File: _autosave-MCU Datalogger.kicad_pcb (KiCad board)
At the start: 2 copper layers, 50.8 x 31.9 mm, 30 parts, among them J1 Conn_01x04_Pin, J2 Conn_01x04_Pin, J3 Conn_01x09_Pin, J4 Conn_02x03_Odd_Even, U1 24LC1025, U2 24LC1025, U3 ATMEGA328P-AU, U4 DS1337S_, Y1 32.768kHz, Y2 16KHz

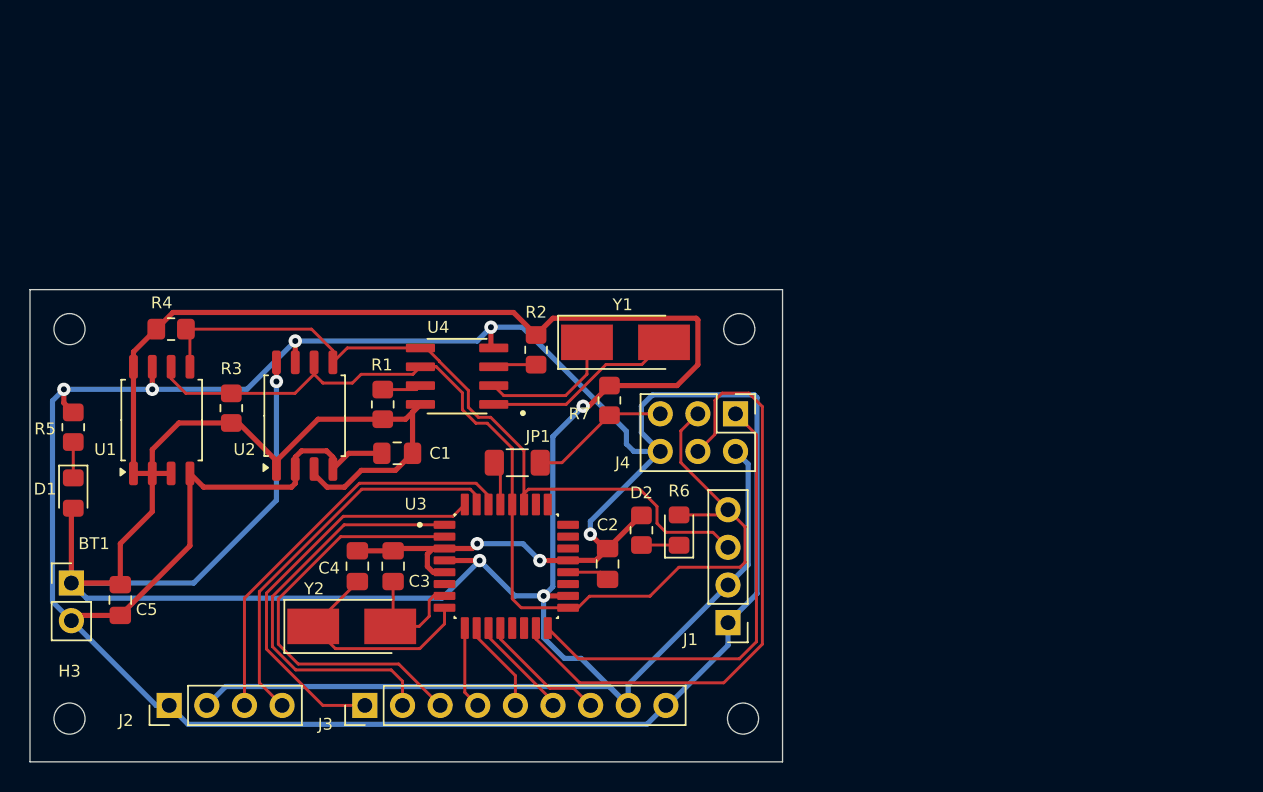
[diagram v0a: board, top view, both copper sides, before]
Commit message: completed the routing of the PCB
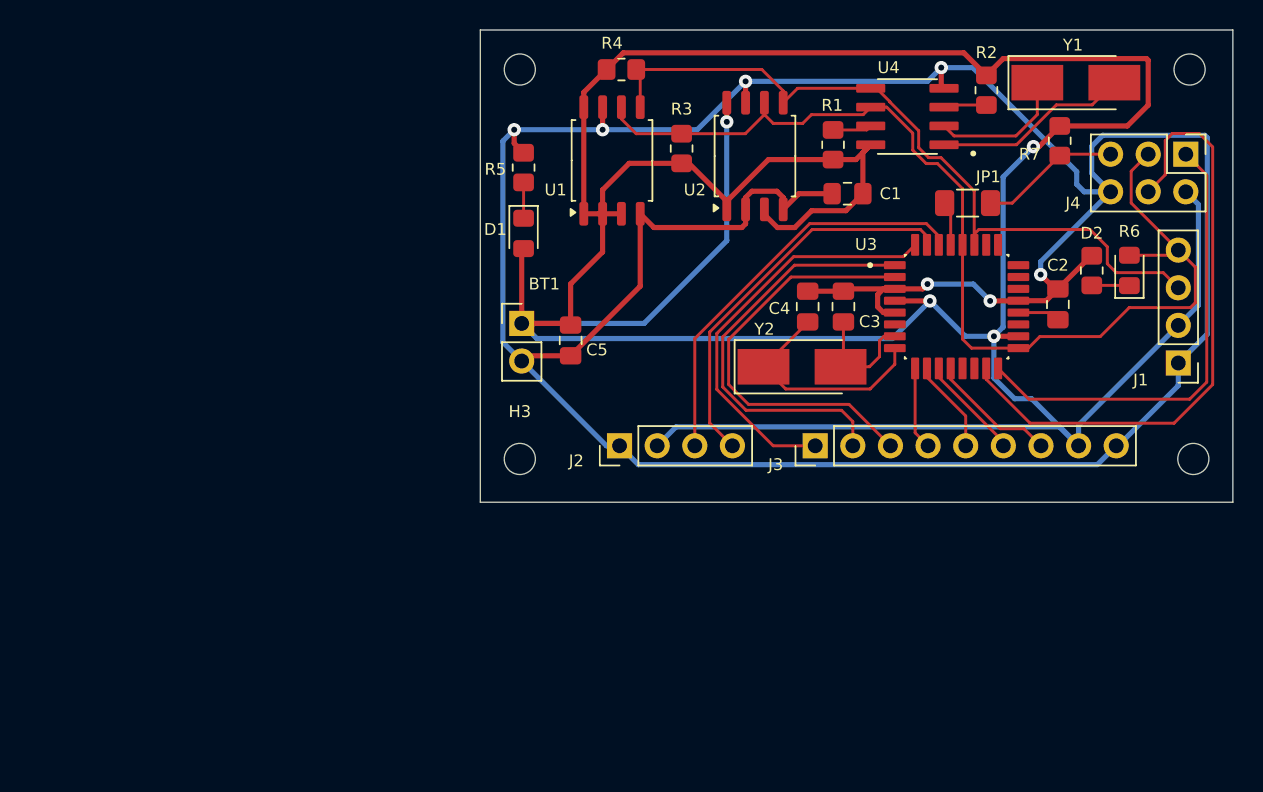
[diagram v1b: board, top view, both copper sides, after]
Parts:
- moved BT1 35.1 mm to (118.0, 102.1)
- moved U1 35.1 mm to (124.1, 91.1)
- moved C2 35.1 mm to (154.2, 100.8)
- moved C3 35.1 mm to (139.7, 101.0)
- moved H1 35.1 mm to (117.9, 85.0)
- moved H2 35.1 mm to (163.1, 85.0)
- moved J2 35.1 mm to (124.6, 110.4)
- moved J3 35.1 mm to (137.8, 110.4)
- moved JP1 35.1 mm to (148.1, 94.0)
- moved R1 35.1 mm to (139.0, 90.0)
- moved R3 35.1 mm to (128.8, 90.3)
- moved R4 35.1 mm to (124.8, 85.0)
- moved R6 35.1 mm to (156.5, 98.5)
- moved R7 35.1 mm to (154.4, 89.8)
- moved U2 35.1 mm to (133.8, 90.8)
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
